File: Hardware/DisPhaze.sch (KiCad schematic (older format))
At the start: 76 parts, among them J1 SWD_Header, J2 PItch_In, J3 PD1_Amt_In, J4 PD2_Amt_In, J5 VCA_In, J6 DAC1_Out, J7 DAC2_Out, J8 Eurorack_16_pin_power, SW1 DAC1_RingMod_Switch, SW2 DAC2_Mix_Switch, SW3 Octave_Switch, U1 STM32F405RGTx, U2 MCP6004, U3 TL072, U4 LM1117-3.3, Y1 Crystal

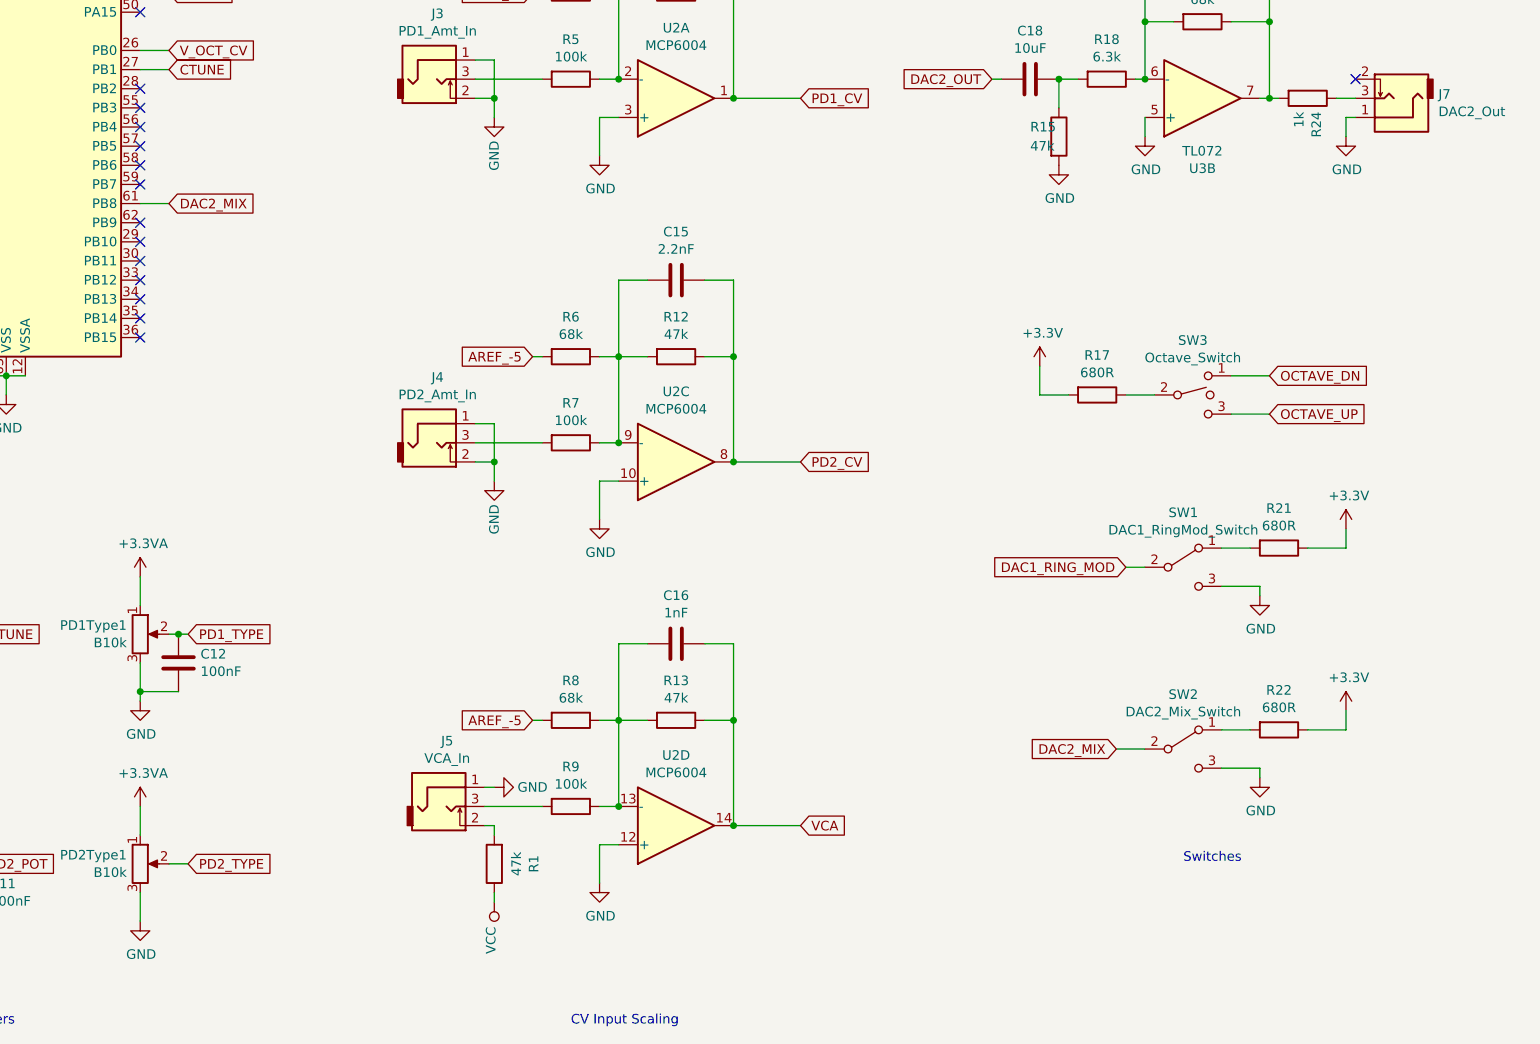
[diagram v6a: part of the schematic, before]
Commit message: Added basic calibration and further tweaks to panel
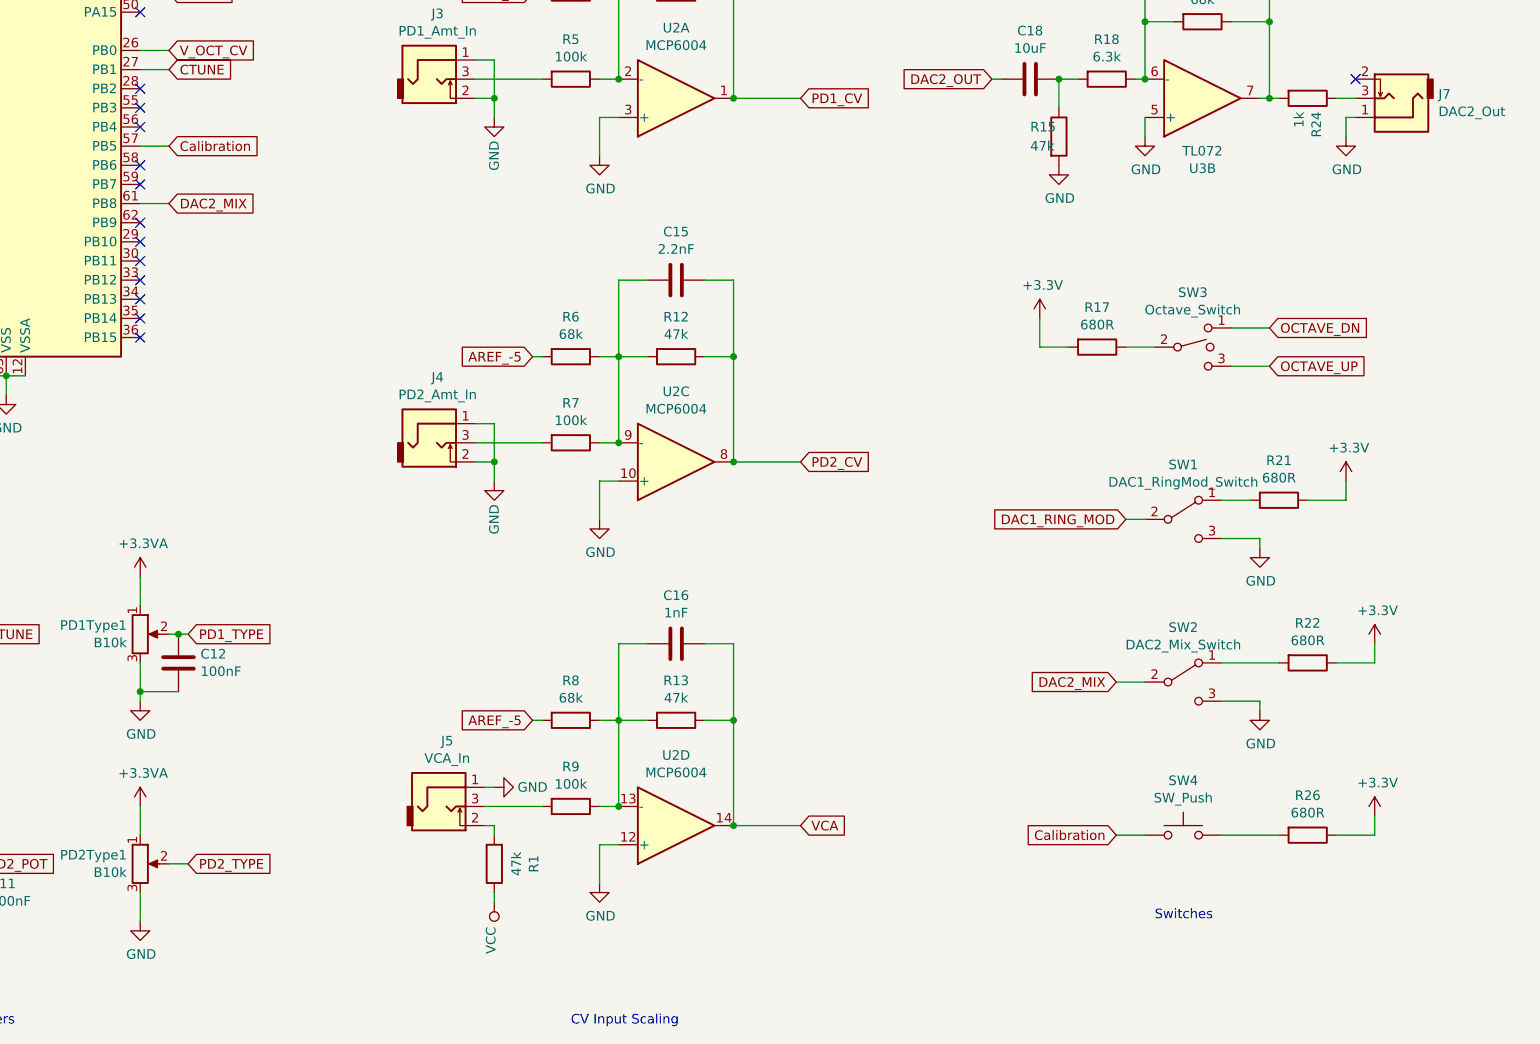
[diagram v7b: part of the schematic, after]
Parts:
- added R26: 680R, Resistors_SMD:R_0805_HandSoldering, symbol Device:R
- added SW4: SW_Push, Buttons_Switches_SMD:SW_SPST_EVQQ2, symbol Switch:SW_Push
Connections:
- net +3V3: now also R26.1
- net Calibration: now reaches U1.57 (PB5)
- net Calibration: now also SW4.1
- new net: R26.2, SW4.2
- no-connect marks 40 -> 39
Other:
- moved on the sheet: R17, R21, R22, SW1, SW2, SW3
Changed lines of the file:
@@
 Wire Wire Line
 	3400 2400 3250 2400
-Text GLabel 8400 6400 0    50   Input ~ 0
+Text GLabel 8400 6150 0    50   Input ~ 0
 DAC1_RING_MOD
 Text GLabel 1650 4300 0    50   Input ~ 0
@@
 L Switch:SW_SPDT_MSM SW3
 U 1 1 5C8C13F5
-P 8750 5500
-F 0 "SW3" H 8750 5785 50  0000 C CNN
-F 1 "Octave_Switch" H 8750 5694 50  0000 C CNN
-F 2 "Custom_Footprints:SPDTSubMiniature" H 8750 5500 50  0001 C CNN
-F 3 "" H 8750 5500 50  0001 C CNN
-	1    8750 5500
+P 8750 5250
+F 0 "SW3" H 8750 5535 50  0000 C CNN
+F 1 "Octave_Switch" H 8750 5444 50  0000 C CNN
+F 2 "Custom_Footprints:SPDTSubMiniature" H 8750 5250 50  0001 C CNN
+F 3 "" H 8750 5250 50  0001 C CNN
+	1    8750 5250
 	1    0    0    -1
 $EndComp
@@
 L Device:R R17
 U 1 1 5C8C15C8
-P 8250 5500
-F 0 "R17" V 8043 5500 50  0000 C CNN
-F 1 "680R" V 8134 5500 50  0000 C CNN
-F 2 "Resistors_SMD:R_0805_HandSoldering" V 8180 5500 50  0001 C CNN
-F 3 "~" H 8250 5500 50  0001 C CNN
-	1    8250 5500
-	0    1    1    0
-$EndComp
-Wire Wire Line
-	8400 5500 8550 5500
+P 8250 5250
+F 0 "R17" V 8043 5250 50  0000 C CNN
+F 1 "680R" V 8134 5250 50  0000 C CNN
+F 2 "Resistors_SMD:R_0805_HandSoldering" V 8180 5250 50  0001 C CNN
+F 3 "~" H 8250 5250 50  0001 C CNN
+	1    8250 5250
+	0    1    1    0
+$EndComp
+Wire Wire Line
+	8400 5250 8550 5250
 $Comp
 L power:+3.3V #PWR032
 U 1 1 5C8C94A6
-P 7950 5350
-F 0 "#PWR032" H 7950 5200 50  0001 C CNN
-F 1 "+3.3V" H 7965 5523 50  0000 C CNN
-F 2 "" H 7950 5350 50  0001 C CNN
-F 3 "" H 7950 5350 50  0001 C CNN
-	1    7950 5350
-	1    0    0    -1
-$EndComp
-Wire Wire Line
-	7950 5350 7950 5500
-Wire Wire Line
-	7950 5500 8100 5500
-Text GLabel 9150 5600 2    50   Input ~ 0
+P 7950 5100
+F 0 "#PWR032" H 7950 4950 50  0001 C CNN
+F 1 "+3.3V" H 7965 5273 50  0000 C CNN
+F 2 "" H 7950 5100 50  0001 C CNN
+F 3 "" H 7950 5100 50  0001 C CNN
+	1    7950 5100
+	1    0    0    -1
+$EndComp
+Wire Wire Line
+	7950 5100 7950 5250
+Wire Wire Line
+	7950 5250 8100 5250
+Text GLabel 9150 5350 2    50   Input ~ 0
 OCTAVE_UP
-Text GLabel 9150 5400 2    50   Input ~ 0
+Text GLabel 9150 5150 2    50   Input ~ 0
 OCTAVE_DN
 Wire Wire Line
-	8950 5400 9150 5400
-Wire Wire Line
-	8950 5600 9150 5600
+	8950 5150 9150 5150
+Wire Wire Line
+	8950 5350 9150 5350
 Text GLabel 1650 4700 0    50   Input ~ 0
 OCTAVE_UP
@@
 L Switch:SW_SPDT SW2
 U 1 1 5CD07DEA
-P 8700 7350
-F 0 "SW2" H 8700 7635 50  0000 C CNN
-F 1 "DAC2_Mix_Switch" H 8700 7544 50  0000 C CNN
-F 2 "Custom_Footprints:SPDTSubMiniature" H 8700 7350 50  0001 C CNN
-F 3 "" H 8700 7350 50  0001 C CNN
-	1    8700 7350
-	1    0    0    -1
-$EndComp
-Text GLabel 8350 7350 0    50   Input ~ 0
+P 8700 7000
+F 0 "SW2" H 8700 7285 50  0000 C CNN
+F 1 "DAC2_Mix_Switch" H 8700 7194 50  0000 C CNN
+F 2 "Custom_Footprints:SPDTSubMiniature" H 8700 7000 50  0001 C CNN
+F 3 "" H 8700 7000 50  0001 C CNN
+	1    8700 7000
+	1    0    0    -1
+$EndComp
+Text GLabel 8350 7000 0    50   Input ~ 0
 DAC2_MIX
 Wire Wire Line
-	8500 7350 8350 7350
+	8500 7000 8350 7000
 $Comp
 L power:GND #PWR038
 U 1 1 5CD173A8
-P 9100 7500
-F 0 "#PWR038" H 9100 7250 50  0001 C CNN
-F 1 "GND" H 9105 7327 50  0000 C CNN
-F 2 "" H 9100 7500 50  0001 C CNN
-F 3 "" H 9100 7500 50  0001 C CNN
-	1    9100 7500
-	1    0    0    -1
-$EndComp
-Wire Wire Line
-	8900 7450 9100 7450
-Wire Wire Line
-	9100 7450 9100 7500
+P 9100 7150
+F 0 "#PWR038" H 9100 6900 50  0001 C CNN
+F 1 "GND" H 9105 6977 50  0000 C CNN
+F 2 "" H 9100 7150 50  0001 C CNN
+F 3 "" H 9100 7150 50  0001 C CNN
+	1    9100 7150
+	1    0    0    -1
+$EndComp
+Wire Wire Line
+	8900 7100 9100 7100
+Wire Wire Line
+	9100 7100 9100 7150
 $Comp
 L Device:R R22
 U 1 1 5CD265CD
-P 9200 7250
-F 0 "R22" V 8993 7250 50  0000 C CNN
-F 1 "680R" V 9084 7250 50  0000 C CNN
-F 2 "Resistors_SMD:R_0805_HandSoldering" V 9130 7250 50  0001 C CNN
-F 3 "~" H 9200 7250 50  0001 C CNN
-	1    9200 7250
+P 9350 6900
+F 0 "R22" V 9143 6900 50  0000 C CNN
+F 1 "680R" V 9234 6900 50  0000 C CNN
+F 2 "Resistors_SMD:R_0805_HandSoldering" V 9280 6900 50  0001 C CNN
+F 3 "~" H 9350 6900 50  0001 C CNN
+	1    9350 6900
 	0    1    1    0
 $EndComp
@@
 L power:+3.3V #PWR042
 U 1 1 5CD265D3
-P 9550 7150
-F 0 "#PWR042" H 9550 7000 50  0001 C CNN
-F 1 "+3.3V" H 9565 7323 50  0000 C CNN
-F 2 "" H 9550 7150 50  0001 C CNN
-F 3 "" H 9550 7150 50  0001 C CNN
-	1    9550 7150
-	1    0    0    -1
-$EndComp
-Wire Wire Line
-	9550 7150 9550 7250
-Wire Wire Line
-	9550 7250 9350 7250
-Wire Wire Line
-	8900 7250 9050 7250
+P 9700 6800
+F 0 "#PWR042" H 9700 6650 50  0001 C CNN
+F 1 "+3.3V" H 9715 6973 50  0000 C CNN
+F 2 "" H 9700 6800 50  0001 C CNN
+F 3 "" H 9700 6800 50  0001 C CNN
+	1    9700 6800
+	1    0    0    -1
+$EndComp
+Wire Wire Line
+	9700 6800 9700 6900
+Wire Wire Line
+	9700 6900 9500 6900
 Text GLabel 3400 4500 2    50   Input ~ 0
 DAC2_MIX
@@
 L Switch:SW_SPDT SW1
 U 1 1 5C8CCA11
-P 8700 6400
-F 0 "SW1" H 8700 6685 50  0000 C CNN
-F 1 "DAC1_RingMod_Switch" H 8700 6594 50  0000 C CNN
-F 2 "Custom_Footprints:SPDTSubMiniature" H 8700 6400 50  0001 C CNN
-F 3 "" H 8700 6400 50  0001 C CNN
-	1    8700 6400
-	1    0    0    -1
-$EndComp
-Wire Wire Line
-	8500 6400 8400 6400
+P 8700 6150
+F 0 "SW1" H 8700 6435 50  0000 C CNN
+F 1 "DAC1_RingMod_Switch" H 8700 6344 50  0000 C CNN
+F 2 "Custom_Footprints:SPDTSubMiniature" H 8700 6150 50  0001 C CNN
+F 3 "" H 8700 6150 50  0001 C CNN
+	1    8700 6150
+	1    0    0    -1
+$EndComp
+Wire Wire Line
+	8500 6150 8400 6150
 $Comp
 L power:GND #PWR037
 U 1 1 5C8CCA19
-P 9100 6550
-F 0 "#PWR037" H 9100 6300 50  0001 C CNN
-F 1 "GND" H 9105 6377 50  0000 C CNN
-F 2 "" H 9100 6550 50  0001 C CNN
-F 3 "" H 9100 6550 50  0001 C CNN
-	1    9100 6550
-	1    0    0    -1
-$EndComp
-Wire Wire Line
-	8900 6500 9100 6500
-Wire Wire Line
-	9100 6500 9100 6550
+P 9100 6300
+F 0 "#PWR037" H 9100 6050 50  0001 C CNN
+F 1 "GND" H 9105 6127 50  0000 C CNN
+F 2 "" H 9100 6300 50  0001 C CNN
+F 3 "" H 9100 6300 50  0001 C CNN
+	1    9100 6300
+	1    0    0    -1
+$EndComp
+Wire Wire Line
+	8900 6250 9100 6250
+Wire Wire Line
+	9100 6250 9100 6300
 $Comp
 L Device:R R21
 U 1 1 5C8CCA21
-P 9200 6300
-F 0 "R21" V 8993 6300 50  0000 C CNN
-F 1 "680R" V 9084 6300 50  0000 C CNN
-F 2 "Resistors_SMD:R_0805_HandSoldering" V 9130 6300 50  0001 C CNN
-F 3 "~" H 9200 6300 50  0001 C CNN
-	1    9200 6300
+P 9200 6050
+F 0 "R21" V 8993 6050 50  0000 C CNN
+F 1 "680R" V 9084 6050 50  0000 C CNN
+F 2 "Resistors_SMD:R_0805_HandSoldering" V 9130 6050 50  0001 C CNN
+F 3 "~" H 9200 6050 50  0001 C CNN
+	1    9200 6050
 	0    1    1    0
 $EndComp
@@
 L power:+3.3V #PWR041
 U 1 1 5C8CCA27
-P 9550 6200
-F 0 "#PWR041" H 9550 6050 50  0001 C CNN
-F 1 "+3.3V" H 9565 6373 50  0000 C CNN
-F 2 "" H 9550 6200 50  0001 C CNN
-F 3 "" H 9550 6200 50  0001 C CNN
-	1    9550 6200
-	1    0    0    -1
-$EndComp
-Wire Wire Line
-	9550 6200 9550 6300
-Wire Wire Line
-	9550 6300 9350 6300
-Wire Wire Line
-	8900 6300 9050 6300
+P 9550 5950
+F 0 "#PWR041" H 9550 5800 50  0001 C CNN
+F 1 "+3.3V" H 9565 6123 50  0000 C CNN
+F 2 "" H 9550 5950 50  0001 C CNN
+F 3 "" H 9550 5950 50  0001 C CNN
+	1    9550 5950
+	1    0    0    -1
+$EndComp
+Wire Wire Line
+	9550 5950 9550 6050
+Wire Wire Line
+	9550 6050 9350 6050
+Wire Wire Line
+	8900 6050 9050 6050
 Wire Wire Line
 	700  3100 700  3400
@@
 Text Notes 8450 800  0    50   ~ 0
 Output Amplifiers
-Text Notes 8700 7950 0    50   ~ 0
+Text Notes 8550 8250 0    50   ~ 0
 Switches
 $Comp
@@
 NoConn ~ 3250 4400
 NoConn ~ 3250 4300
-NoConn ~ 3250 4200
 NoConn ~ 3250 4100
 NoConn ~ 3250 4000
@@
 NoConn ~ 3250 5000
 NoConn ~ 3250 4900
+Text GLabel 8350 7800 0    50   Input ~ 0
+Calibration
+$Comp
+L Switch:SW_Push SW4
+U 1 1 5C9B2C11
+P 8700 7800
+F 0 "SW4" H 8700 8085 50  0000 C CNN
+F 1 "SW_Push" H 8700 7994 50  0000 C CNN
+F 2 "Buttons_Switches_SMD:SW_SPST_EVQQ2" H 8700 8000 50  0001 C CNN
+F 3 "" H 8700 8000 50  0001 C CNN
+	1    8700 7800
+	1    0    0    -1
+$EndComp
+Wire Wire Line
+	8350 7800 8500 7800
+Text GLabel 3400 4200 2    50   Input ~ 0
+Calibration
+Wire Wire Line
+	3250 4200 3400 4200
+Wire Wire Line
+	8900 6900 9200 6900
+$Comp
+L Device:R R26
+U 1 1 5CA698C8
+P 9350 7800
+F 0 "R26" V 9143 7800 50  0000 C CNN
+F 1 "680R" V 9234 7800 50  0000 C CNN
+F 2 "Resistors_SMD:R_0805_HandSoldering" V 9280 7800 50  0001 C CNN
+F 3 "~" H 9350 7800 50  0001 C CNN
+	1    9350 7800
+	0    1    1    0
+$EndComp
+$Comp
+L power:+3.3V #PWR0103
+U 1 1 5CA698CE
+P 9700 7700
+F 0 "#PWR0103" H 9700 7550 50  0001 C CNN
+F 1 "+3.3V" H 9715 7873 50  0000 C CNN
+F 2 "" H 9700 7700 50  0001 C CNN
+F 3 "" H 9700 7700 50  0001 C CNN
+	1    9700 7700
+	1    0    0    -1
+$EndComp
+Wire Wire Line
+	9700 7700 9700 7800
+Wire Wire Line
+	9700 7800 9500 7800
+Wire Wire Line
+	8900 7800 9200 7800
 $EndSCHEMATC
